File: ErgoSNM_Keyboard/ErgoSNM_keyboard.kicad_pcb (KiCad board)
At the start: 2 copper layers, 96 parts, among them J1 Conn_01x13, J2 Conn_01x13, J3 Conn_01x03, J4 Conn_01x04, SW1 RESET, SW2 SW_2P2T

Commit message: Update PCB
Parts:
- added J3: Conn_01x06, Connector_PinHeader_2.54mm:PinHeader_1x06_P2.54mm_Vertical, F.Cu at (201.9, 52.1)
- added J5: Conn_01x07, Connector_PinHeader_2.54mm:PinHeader_1x07_P2.54mm_Vertical, F.Cu at (177.3, 119.7)
- added J7: Conn_01x07, Connector_PinHeader_2.54mm:PinHeader_1x07_P2.54mm_Vertical, F.Cu at (168.8, 112.9)
- added REF**: MountingHole_3.2mm_M3, MountingHole:MountingHole_3.2mm_M3, F.Cu at (185.8, 65.2)
- added REF**: MountingHole_3.2mm_M3, MountingHole:MountingHole_3.2mm_M3, F.Cu at (185.7, 49.4)
- added REF**: MountingHole_3.2mm_M3, MountingHole:MountingHole_3.2mm_M3, F.Cu at (123.1, 106.3)
- added REF**: MountingHole_3.2mm_M3, MountingHole:MountingHole_3.2mm_M3, F.Cu at (209.9, 141.8)
- added REF**: MountingHole_3.2mm_M3, MountingHole:MountingHole_3.2mm_M3, F.Cu at (85.7, 112.6)
- added REF**: MountingHole_3.2mm_M3, MountingHole:MountingHole_3.2mm_M3, F.Cu at (170.4, 120.7)
- added REF**: MountingHole_3.2mm_M3, MountingHole:MountingHole_3.2mm_M3, F.Cu at (189.6, 105.5)
- added REF**: MountingHole_3.2mm_M3, MountingHole:MountingHole_3.2mm_M3, F.Cu at (235.2, 131.6)
- added REF**: MountingHole_3.2mm_M3, MountingHole:MountingHole_3.2mm_M3, F.Cu at (161.9, 53.0)
- added REF**: MountingHole_3.2mm_M3, MountingHole:MountingHole_3.2mm_M3, F.Cu at (85.8, 55.5)
- added REF**: MountingHole_3.2mm_M3, MountingHole:MountingHole_3.2mm_M3, F.Cu at (123.5, 48.8)
- added REF**: MountingHole_3.2mm_M3, MountingHole:MountingHole_3.2mm_M3, F.Cu at (165.0, 110.6)
- added REF**: MountingHole_3.2mm_M3, MountingHole:MountingHole_3.2mm_M3, F.Cu at (104.4, 72.7)
- added REF**: MountingHole_3.2mm_M3, MountingHole:MountingHole_3.2mm_M3, F.Cu at (168.5, 124.2)
- added REF**: MountingHole_3.2mm_M3, MountingHole:MountingHole_3.2mm_M3, F.Cu at (142.8, 88.6)
- J6: renamed from J3; footprint Connector_JST:JST_PH_B2B-PH-K_1x02_P2.00mm_Vertical -> Connector_JST:JST_PH_B3B-PH-K_1x03_P2.00mm_Vertical
- moved TP13 46.1 mm to (194.0, 61.4)
- moved D34 40.3 mm to (219.4, 161.1)
- moved KEY7 38.1 mm to (192.2, 115.2)
- moved KEY34 38.1 mm to (215.7, 150.7)
- moved D7 36.2 mm to (195.9, 125.5)
- moved D14 27.2 mm to (212.4, 135.0)
- moved D35 27.2 mm to (202.9, 151.5)
- moved J4 27.1 mm to (196.2, 87.6), turned to -90 degrees
- moved KEY14 26.9 mm to (208.7, 124.7)
- moved KEY35 26.9 mm to (199.2, 141.2)
- moved D21 21.3 mm to (228.9, 144.6)
- moved KEY28 19.1 mm to (182.7, 131.7)
- moved KEY21 19.1 mm to (225.2, 134.2)
- moved D28 17.2 mm to (186.4, 142.0)
- moved TP2 10.3 mm to (76.2, 72.4)
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- renumbered D11 to D10, D12 to D11, D13 to D12, D14 to D13, D15 to D14, D16 to D15, D17 to D16, D18 to D17, D19 to D18, D20 to D19, D21 to D20, D22 to D21, D23 to D22, D24 to D23, D25 to D24, D26 to D25, D27 to D26, D28 to D27, D29 to D28, D30 to D29, D31 to D30, D32 to D31, D33 to D32, D34 to D33, D35 to D34, D36 to D35, D9 to D8, D10 to D9, D8 to LD1, TP11 to TP10, TP12 to TP11, TP13 to TP12, TP14 to TP13, TP6 to TP14, TP5 to TP4, TP7 to TP5, TP4 to TP6, TP8 to TP7, TP9 to TP8, TP10 to TP9
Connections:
- J4 pad 1: CS -> VCC
- J4 pad 2: MOSI -> GND
- J4 pad 3: MISO -> COL_6
- J4 pad 4: SCLK -> SCL
- R3 pad 2: SDA -> SCL
- R4 pad 1: SCL -> SDA
- TP14 pad 1: SCL -> SDA
- TP6 pad 1: SDA -> SCL
- TRRS1 pad 2: SCL -> SDA
- TRRS1 pad 3: SDA -> SCL
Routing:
- net ROW_2: track 0.00 -> 307.1 mm, vias 0 -> 1
- net COL_6: track 0.00 -> 295.7 mm, vias 0 -> 1
- net ROW_1: track 0.00 -> 292.6 mm, vias 0 -> 1
- net ROW_0: track 0.00 -> 265.9 mm, vias 0 -> 1
- net ROW_4: track 0.00 -> 252.6 mm
- net ROW_3: track 0.00 -> 216.9 mm
- net COL_0: track 153.3 -> 312.2 mm
- net COL_5: track 122.7 -> 274.2 mm
- net GND: track 0.00 -> 147.4 mm, vias 0 -> 23
- net COL_1: track 154.6 -> 293.5 mm
- net COL_2: track 153.5 -> 274.6 mm
- net COL_3: track 154.6 -> 254.0 mm
- net VCC: track 0.00 -> 77.8 mm, vias 0 -> 1
- net RESET: track 0.00 -> 73.0 mm, vias 0 -> 1
- net COL_4: track 154.4 -> 225.7 mm
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- added copper zone on B.Cu, net (none)
- added copper zone on F.Cu, net (none)
- added copper zone on B.Cu, net GND
- added copper zone on F.Cu, net GND
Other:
- board outline added: 173.1 x 137.3 mm

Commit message: Add mark
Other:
- board text added: "ErgoSNM v${REVISION}"

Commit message: Update footprint
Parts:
- removed the REF** at (185.8, 65.2)
- removed the REF** at (185.7, 49.4)
- removed the REF** at (123.1, 106.3)
- removed the REF** at (209.9, 141.8)
- removed the REF** at (85.7, 112.6)
- removed the REF** at (189.6, 105.5)
- removed the REF** at (235.2, 131.6)
- removed the REF** at (161.9, 53.0)
- removed the REF** at (123.5, 48.8)
- removed the REF** at (165.0, 110.6)
- removed the REF** at (104.4, 72.7)
- removed the REF** at (142.8, 88.6)
- added REF**: MountingHole_2.2mm_M2, MountingHole:MountingHole_2.2mm_M2, F.Cu at (123.8, 105.4)
- added REF**: MountingHole_2.2mm_M2, MountingHole:MountingHole_2.2mm_M2, F.Cu at (185.8, 65.2)
- added REF**: MountingHole_2.2mm_M2, MountingHole:MountingHole_2.2mm_M2, F.Cu at (185.7, 49.4)
- added REF**: MountingHole_2.2mm_M2, MountingHole:MountingHole_2.2mm_M2, F.Cu at (142.9, 85.7)
- added REF**: MountingHole_2.2mm_M2, MountingHole:MountingHole_2.2mm_M2, F.Cu at (85.7, 111.1)
- added REF**: MountingHole_2.2mm_M2, MountingHole:MountingHole_2.2mm_M2, F.Cu at (161.9, 50.2)
- added REF**: MountingHole_2.2mm_M2, MountingHole:MountingHole_2.2mm_M2, F.Cu at (235.2, 131.6)
- added REF**: MountingHole_2.2mm_M2, MountingHole:MountingHole_2.2mm_M2, F.Cu at (209.9, 141.8)
- added REF**: MountingHole_2.2mm_M2, MountingHole:MountingHole_2.2mm_M2, F.Cu at (165.1, 110.5)
- added REF**: MountingHole_2.2mm_M2, MountingHole:MountingHole_2.2mm_M2, F.Cu at (189.6, 105.5)
- added REF**: MountingHole_2.2mm_M2, MountingHole:MountingHole_2.2mm_M2, F.Cu at (123.8, 48.3)
- added REF**: MountingHole_2.2mm_M2, MountingHole:MountingHole_2.2mm_M2, F.Cu at (104.4, 72.7)
- REF**: value MountingHole_3.2mm_M3 -> MountingHole_2.2mm_M2; footprint MountingHole:MountingHole_3.2mm_M3 -> MountingHole:MountingHole_2.2mm_M2
- moved REF** 1.52 mm to (85.8, 54.0)
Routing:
- net ROW_0: track 265.9 -> 268.1 mm
- net ROW_3: track 216.9 -> 218.1 mm

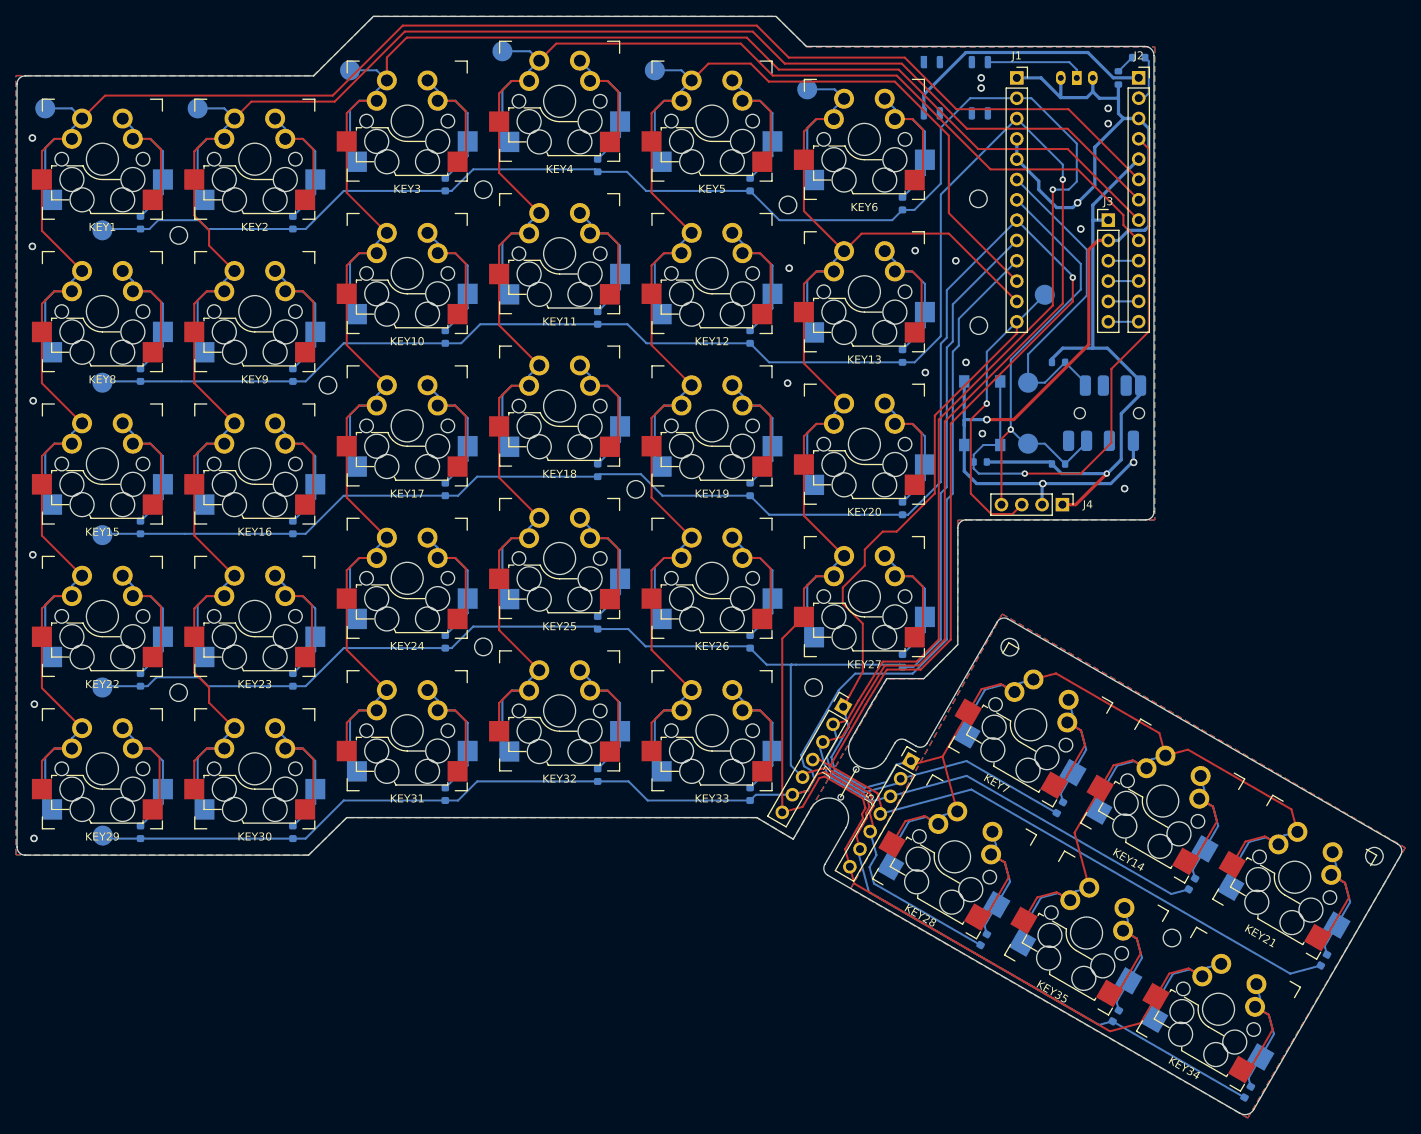
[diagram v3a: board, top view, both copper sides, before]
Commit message: Move 1N4148s away from key switches
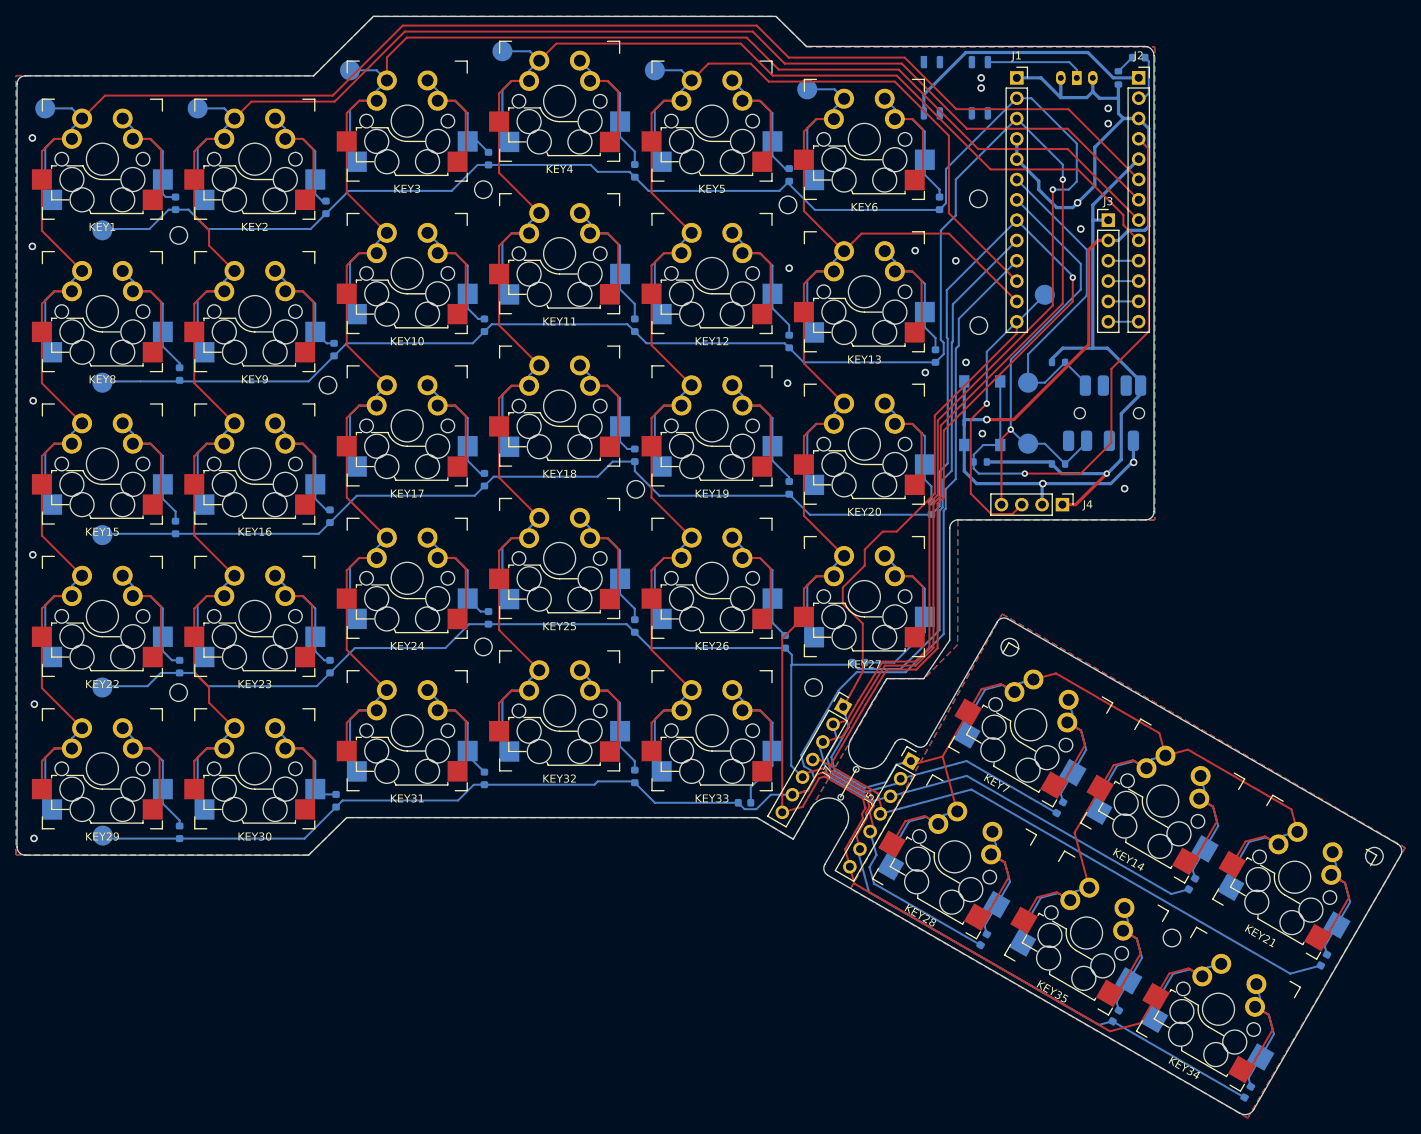
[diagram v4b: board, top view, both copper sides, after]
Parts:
- moved D30 6.68 mm to (105.4, 124.6)
- moved D3 6.30 mm to (124.5, 44.4)
- moved D24 6.17 mm to (124.5, 101.8)
- moved D9 6.05 mm to (105.2, 68.3)
- moved D27 5.53 mm to (170.7, 107.4), turned to 0 degrees
- moved D31 5.27 mm to (124.0, 121.8)
- moved D22 5.16 mm to (85.9, 107.9)
- moved D10 5.10 mm to (124.0, 65.2)
- moved D5 5.04 mm to (162.1, 46.4)
- moved D17 5.04 mm to (124.0, 84.5)
- moved D1 5.01 mm to (85.3, 50.0)
- moved D18 5.00 mm to (142.7, 81.5)
- moved D23 4.92 mm to (104.6, 107.9)
- moved D12 4.92 mm to (162.1, 67.2)
- moved D19 4.89 mm to (162.1, 85.5)
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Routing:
- net Net-(D27-Pad2): track 27.6 -> 32.8 mm
- net ROW_2: track 307.4 -> 310.8 mm
- net Net-(D30-Pad2): track 27.5 -> 24.6 mm
- net Net-(D9-Pad2): track 27.5 -> 24.7 mm
- net Net-(D3-Pad2): track 27.5 -> 24.9 mm
- net Net-(D24-Pad2): track 27.5 -> 25.0 mm
- net Net-(D31-Pad2): track 27.5 -> 25.3 mm
- net Net-(D2-Pad2): track 27.5 -> 25.3 mm
- net Net-(D1-Pad2): track 27.5 -> 25.3 mm
- net Net-(D33-Pad2): track 27.5 -> 29.4 mm
- net Net-(D18-Pad2): track 27.6 -> 25.9 mm
- net Net-(D23-Pad2): track 27.4 -> 25.7 mm
- net ROW_1: track 292.6 -> 294.1 mm
- net Net-(D16-Pad2): track 27.5 -> 26.0 mm
- net Net-(D22-Pad2): track 27.5 -> 26.1 mm
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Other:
- outline, holes or cut-outs redrawn
